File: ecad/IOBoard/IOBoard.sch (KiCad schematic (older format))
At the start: 7 parts

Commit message: Add IOBoard
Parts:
- removed BT?: 9V Bat, symbol Device:Battery
- removed J?: Barrel_Jack_Switch, symbol Connector:Barrel_Jack_Switch
- removed J?: Input, symbol Connector:Barrel_Jack_Switch
- removed J?: 9VDC, symbol Connector:Barrel_Jack
- removed U? (x3): SW_3PST, symbol Switch:SW_3PST
- added BAT?: BC9VPC, digikey-footprints:Battery_Holder_9V_BC9VPC-ND, symbol dk_Battery-Holders-Clips-Contacts:BC9VPC
- added C?: 10u, symbol Device:CP
- added C?: 1u, symbol Device:C
- added C?: .1u, symbol Device:C
- added D?: LED, symbol Device:LED
- added J? (x2): SN37A12A, symbol Connector:AudioJack2_Ground_SwitchT
- added J?: PJ-102A, digikey-footprints:Barrel_Jack_5.5mmODx2.1mmID_PJ-102A, symbol dk_Barrel-Power-Connectors:PJ-102A
- added J?: toEffectsBoard, symbol Connector_Generic:Conn_02x02_Counter_Clockwise
- added R?: 1k, Resistor_SMD:R_0603_1608Metric, symbol Device:R
- added U? (x3): FS57003PLT2B2M2QE, symbol screaming-panda:FS57003PLT2B2M2QE
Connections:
- net labels added: BYPASS, EFFECT_OUT, SIG_IN, SIG_OUT
- wire segments 8 -> 59

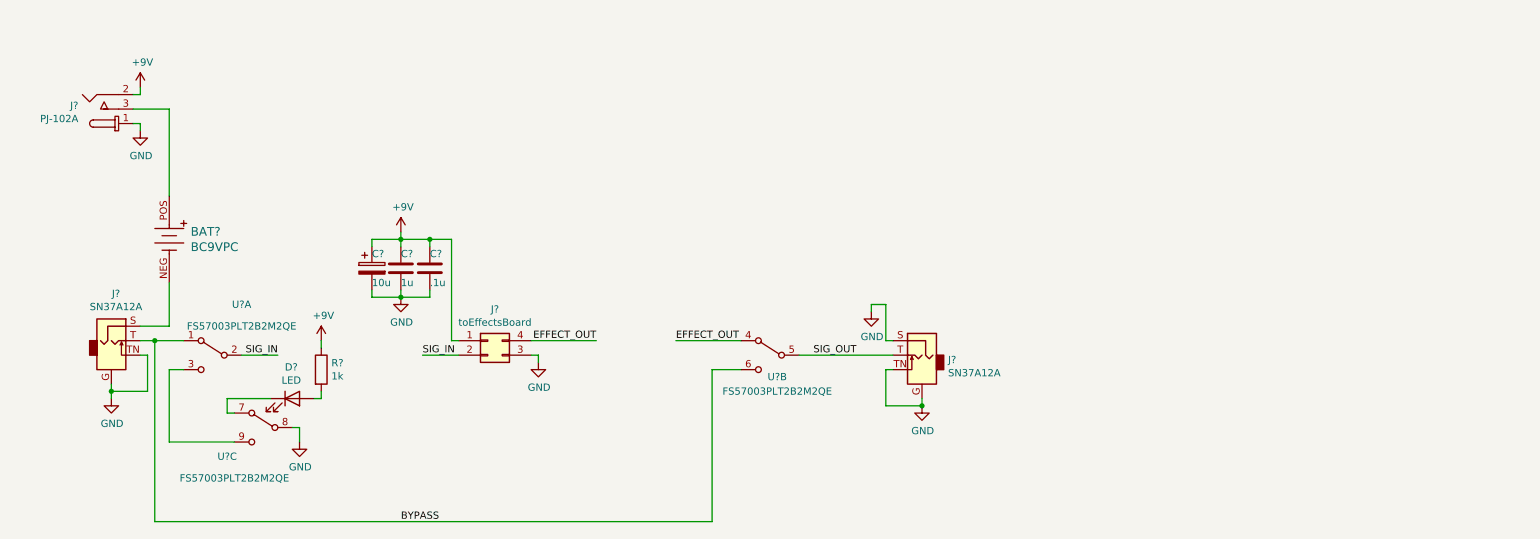
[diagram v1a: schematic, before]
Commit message: Add rev 1.0 EffectsBoard and IOBoard
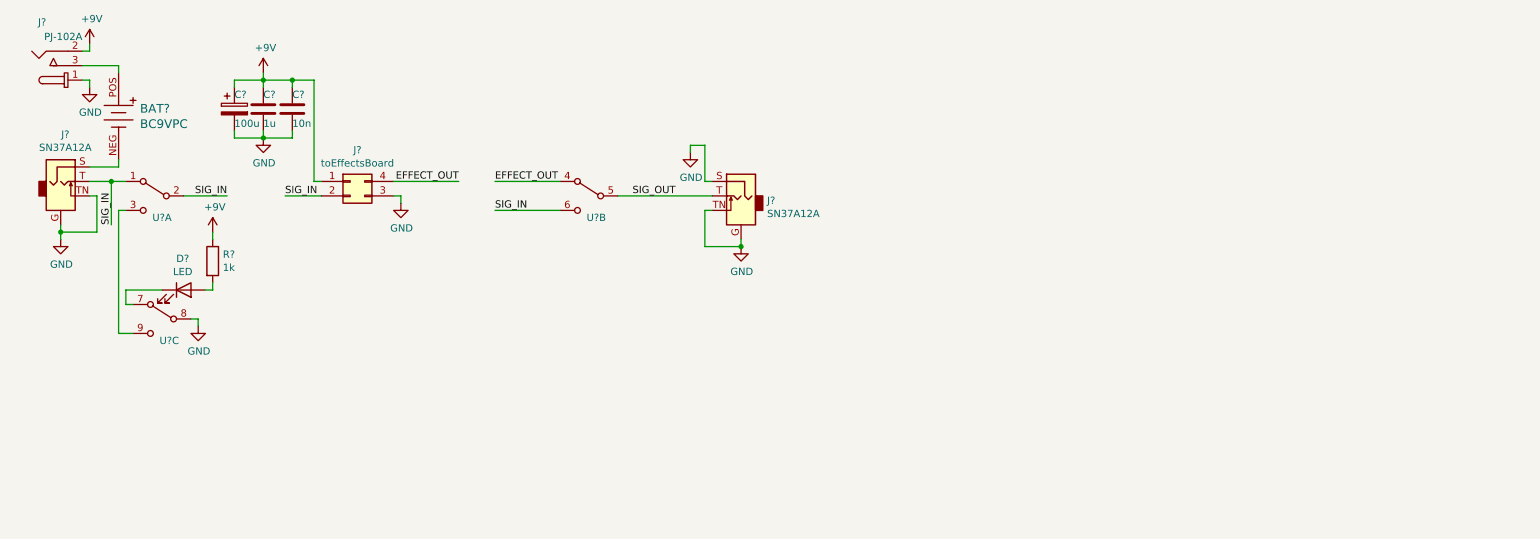
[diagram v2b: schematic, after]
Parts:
- C?: value 10u -> 100u
- C?: value .1u -> 10n
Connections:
- net BYPASS is gone; now on net SIG_IN: J?.T, U?.1, U?.6
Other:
- moved on the sheet: BAT?, C?, D?, J?, R?, U?A, U?B, U?C

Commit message: Update IOBoard
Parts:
- C2, C3: renamed from C?; footprint (none) -> Capacitor_SMD:C_0805_2012Metric_Pad1.18x1.45mm_HandSolder
- D1: renamed from D?; footprint (none) -> Diode_THT:D_DO-201AD_P3.81mm_Vertical_AnodeUp; Spice_Model (none) -> LED; Spice_Netlist_Enabled (none) -> Y; Spice_Primitive (none) -> D
- J1: renamed from J?; Spice_Model (none) -> SN37A12A; Spice_Netlist_Enabled (none) -> N; Spice_Primitive (none) -> J
- J2: renamed from J?; Spice_Model (none) -> dc 9; Spice_Netlist_Enabled (none) -> N; Spice_Primitive (none) -> V
- J3: renamed from J?; footprint (none) -> Connector_PinHeader_1.27mm:PinHeader_2x02_P1.27mm_Vertical
- R1: renamed from R?; footprint Resistor_SMD:R_0603_1608Metric -> Resistor_SMD:R_0805_2012Metric_Pad1.20x1.40mm_HandSolder; Spice_Model (none) -> 1k; Spice_Netlist_Enabled (none) -> Y; Spice_Primitive (none) -> R
- U1: renamed from U?; footprint (none) -> Button_Switch_THT:SW_PUSH_E-Switch_FS5700DP_DPDT
- gave numbers to parts that had none: 3
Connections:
- net EFFECT_OUT: now also U1.7; no longer U1.4
- net GND: now also U1.5; no longer U1.8
- net SIG_IN: now also U1.9; no longer U1.6
- net SIG_OUT: now also U1.8; no longer U1.5
- net at U1.3: now also U1.6; no longer U1.9
- net at D1.1 (K): now also U1.4; no longer U1.7

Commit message: Update bom
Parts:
- C1: footprint (none) -> Capacitor_SMD:C_0805_2012Metric_Pad1.18x1.45mm_HandSolder
- J1, J4: footprint (none) -> screaming-panda:SN37A
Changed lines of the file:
@@
 F 0 "J1" H 732 1975 50  0000 C CNN
 F 1 "SN37A12A" H 732 1884 50  0000 C CNN
-F 2 "" H 700 1650 50  0001 C CNN
+F 2 "screaming-panda:SN37A" H 700 1650 50  0001 C CNN
 F 3 "https://www.switchcraft.com/Documents/Jack_Schematics.pdf" H 700 1650 50  0001 C CNN
 F 4 "J" H 700 1650 50  0001 C CNN "Spice_Primitive"
@@
 F 0 "J4" H 5220 1718 50  0000 R CNN
 F 1 "SN37A12A" H 5220 1627 50  0000 R CNN
-F 2 "" H 5400 1750 50  0001 C CNN
+F 2 "screaming-panda:SN37A" H 5400 1750 50  0001 C CNN
 F 3 "https://www.switchcraft.com/Documents/Jack_Schematics.pdf" H 5400 1750 50  0001 C CNN
 	1    5400 1750
@@
 F 0 "C1" H 1900 1250 50  0000 L CNN
 F 1 "100u" H 1900 1050 50  0000 L CNN
-F 2 "" H 1938 1000 50  0001 C CNN
+F 2 "Capacitor_SMD:C_0805_2012Metric_Pad1.18x1.45mm_HandSolder" H 1938 1000 50  0001 C CNN
 F 3 "~" H 1900 1150 50  0001 C CNN
 	1    1900 1150

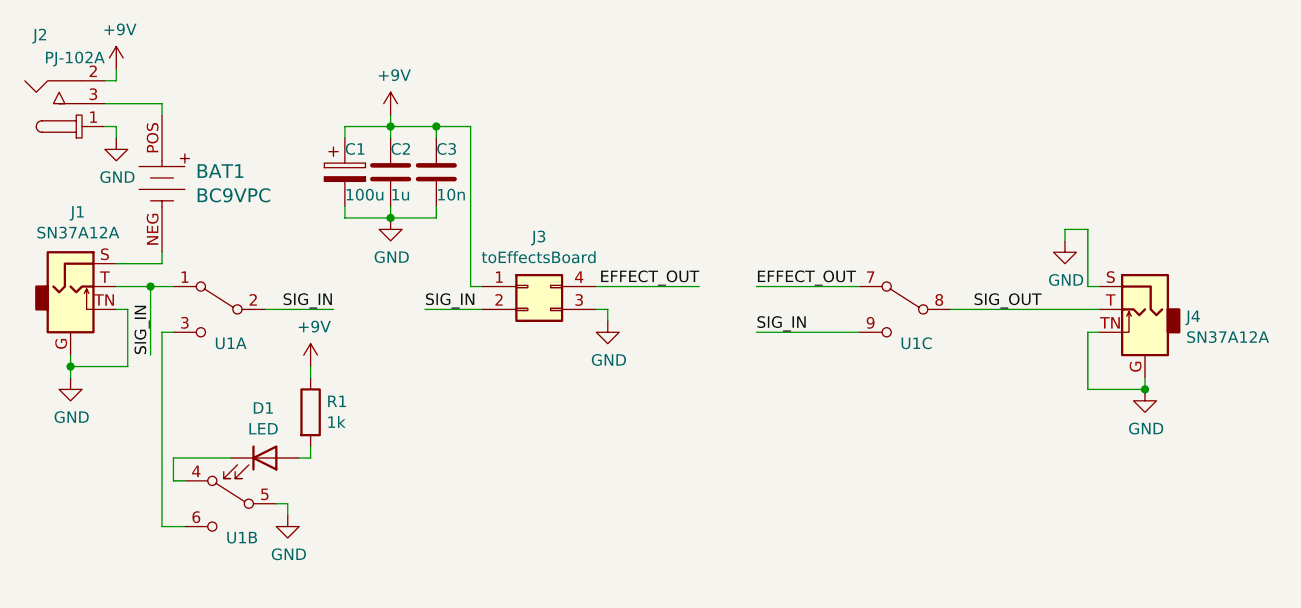
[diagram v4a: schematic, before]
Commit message: Update libraries and CAD
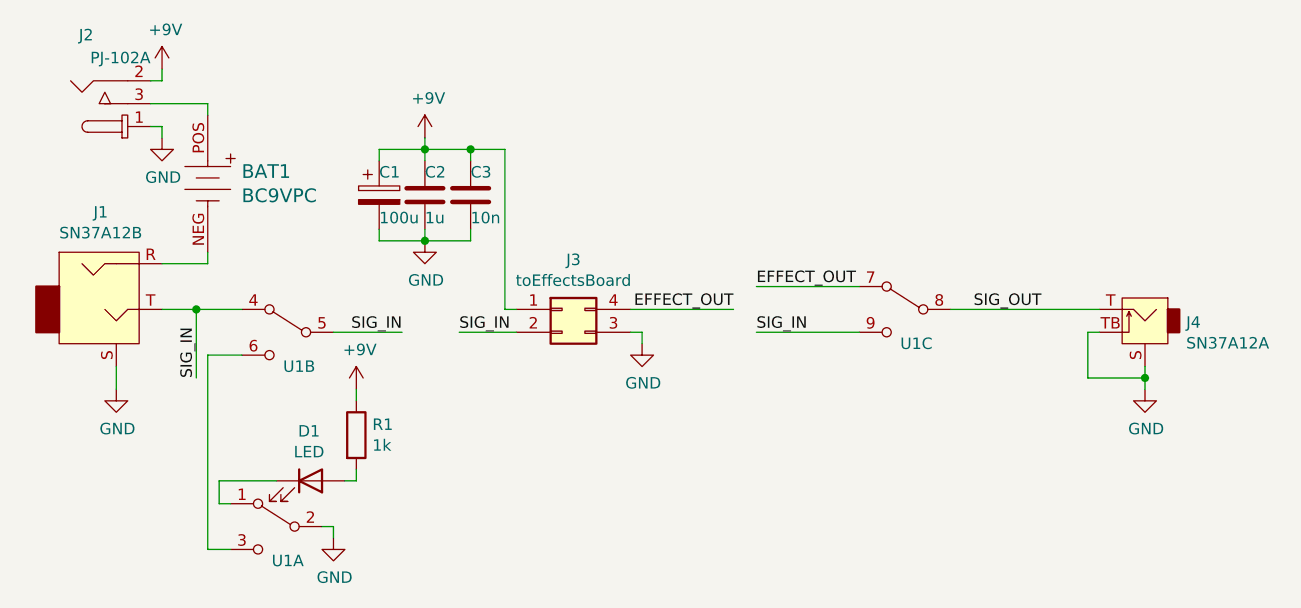
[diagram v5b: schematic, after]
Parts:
- removed J1, J4: SN37A12A, screaming-panda:SN37A, symbol Connector:AudioJack2_Ground_SwitchT
- added J1: SN37A12B, screaming-panda:Switchcraft_SN37A12B, symbol screaming-panda:SN37A12B
- added J4: SN37A12A, screaming-panda:Switchcraft_SN37A12A, symbol screaming-panda:SN37A12A
- BAT1: footprint digikey-footprints:Battery_Holder_9V_BC9VPC-ND -> DigiKey:Battery_Holder_9V_BC9VPC-ND
- J2: footprint digikey-footprints:Barrel_Jack_5.5mmODx2.1mmID_PJ-102A -> DigiKey:Barrel_Jack_5.5mmODx2.1mmID_PJ-102A
- U1: footprint Button_Switch_THT:SW_PUSH_E-Switch_FS5700DP_DPDT -> screaming-panda:SW_PUSH_E-Switch_FS57003PLT_3PDT
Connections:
- net GND: now also U1.2, J1.S, J4.S, J4.TB; no longer U1.5
- net SIG_IN: now also U1.4, U1.5, J1.T; no longer U1.1, U1.2
- net SIG_OUT: now also J4.T
- net at BAT1.NEG: now also J1.R
- net at D1.1 (K): now also U1.1; no longer U1.4
- new net: U1.3, U1.6
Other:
- moved on the sheet: BAT1, C1, C2, C3, D1, J2, J3, R1

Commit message: Route IOBoard
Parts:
- BAT1: footprint DigiKey:Battery_Holder_9V_BC9VPC-ND -> DigiKey:PinHeader_1x2_P2.54mm
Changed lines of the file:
@@
 F 0 "BAT1" V 1247 1348 60  0000 L CNN
 F 1 "BC9VPC" V 1353 1348 60  0000 L CNN
-F 2 "DigiKey:Battery_Holder_9V_BC9VPC-ND" H 1500 1400 60  0001 L CNN
+F 2 "DigiKey:PinHeader_1x2_P2.54mm" H 1500 1400 60  0001 L CNN
 F 3 "http://www.memoryprotectiondevices.com/datasheets/BC9VPC-datasheet.pdf" H 1500 1500 60  0001 L CNN
 F 4 "BC9VPC-ND" H 1500 1600 60  0001 L CNN "Digi-Key_PN"

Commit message: Add barrel jack 3D step
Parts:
- J2: footprint DigiKey:Barrel_Jack_5.5mmODx2.1mmID_PJ-102A -> screaming-panda:Barrel_Jack_5.5mmODx2.1mmID_PJ-102A
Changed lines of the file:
@@
 F 0 "J2" H 800 550 50  0000 R CNN
 F 1 "PJ-102A" H 1050 650 50  0000 R CNN
-F 2 "DigiKey:Barrel_Jack_5.5mmODx2.1mmID_PJ-102A" H 1150 1150 60  0001 L CNN
+F 2 "screaming-panda:Barrel_Jack_5.5mmODx2.1mmID_PJ-102A" H 1150 1150 60  0001 L CNN
 F 3 "https://www.cui.com/product/resource/digikeypdf/pj-102a.pdf" H 1150 1250 60  0001 L CNN
 F 4 "CP-102A-ND" H 1150 1350 60  0001 L CNN "Digi-Key_PN"

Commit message: Add LED datasheet
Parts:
- D1: value LED -> QBL8XX60D
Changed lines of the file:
@@
 P 1750 2500
 F 0 "D1" H 1743 2717 50  0000 C CNN
-F 1 "LED" H 1743 2626 50  0000 C CNN
+F 1 "QBL8XX60D" H 1743 2626 50  0000 C CNN
 F 2 "Diode_THT:D_DO-201AD_P3.81mm_Vertical_AnodeUp" H 1750 2500 50  0001 C CNN
-F 3 "~" H 1750 2500 50  0001 C CNN
+F 3 "http://www.qt-brightek.com/datasheet/QBL8XX60D.pdf" H 1750 2500 50  0001 C CNN
 F 4 "D" H 1750 2500 50  0001 C CNN "Spice_Primitive"
 F 5 "LED" H 1750 2500 50  0001 C CNN "Spice_Model"
